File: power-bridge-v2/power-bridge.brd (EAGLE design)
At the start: 9.8 x 22.4 mm, 3 parts, among them X2 CON-MA03-2PCB_EDGE

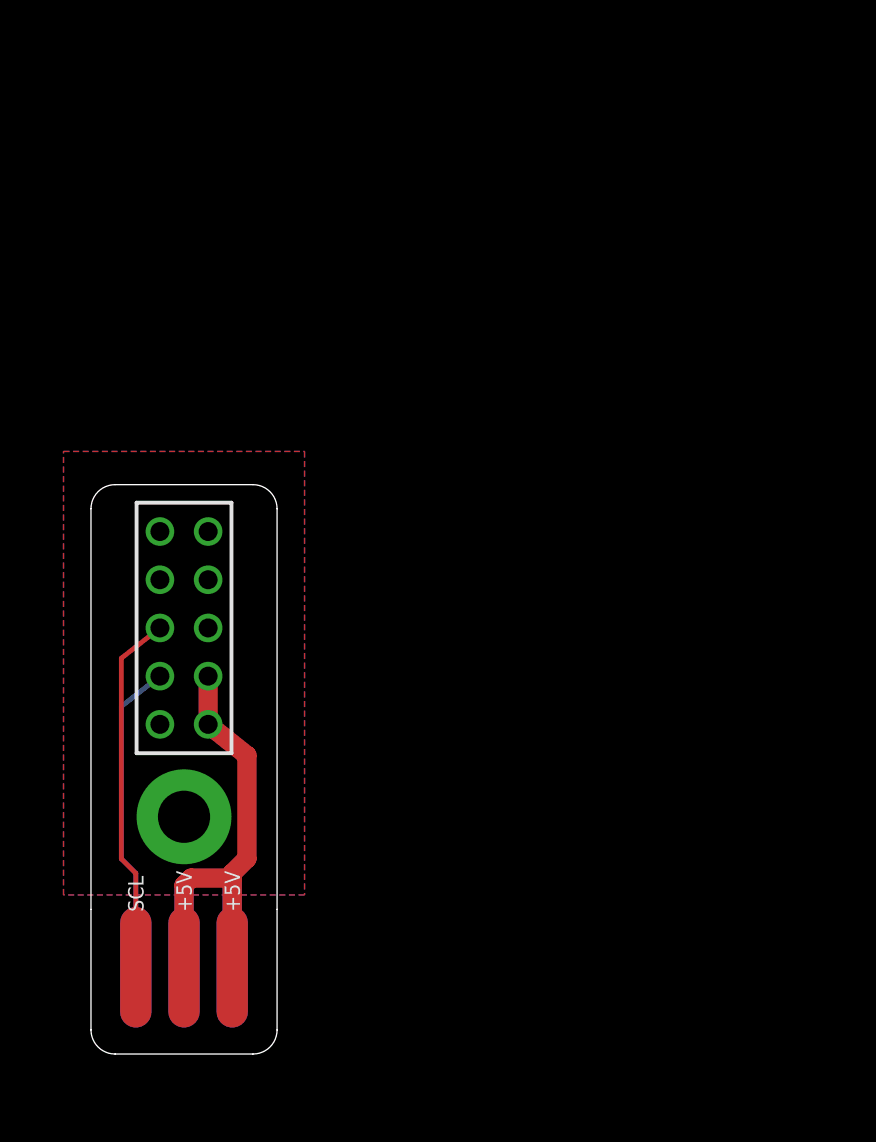
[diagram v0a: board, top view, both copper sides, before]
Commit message: Add power bridge v3
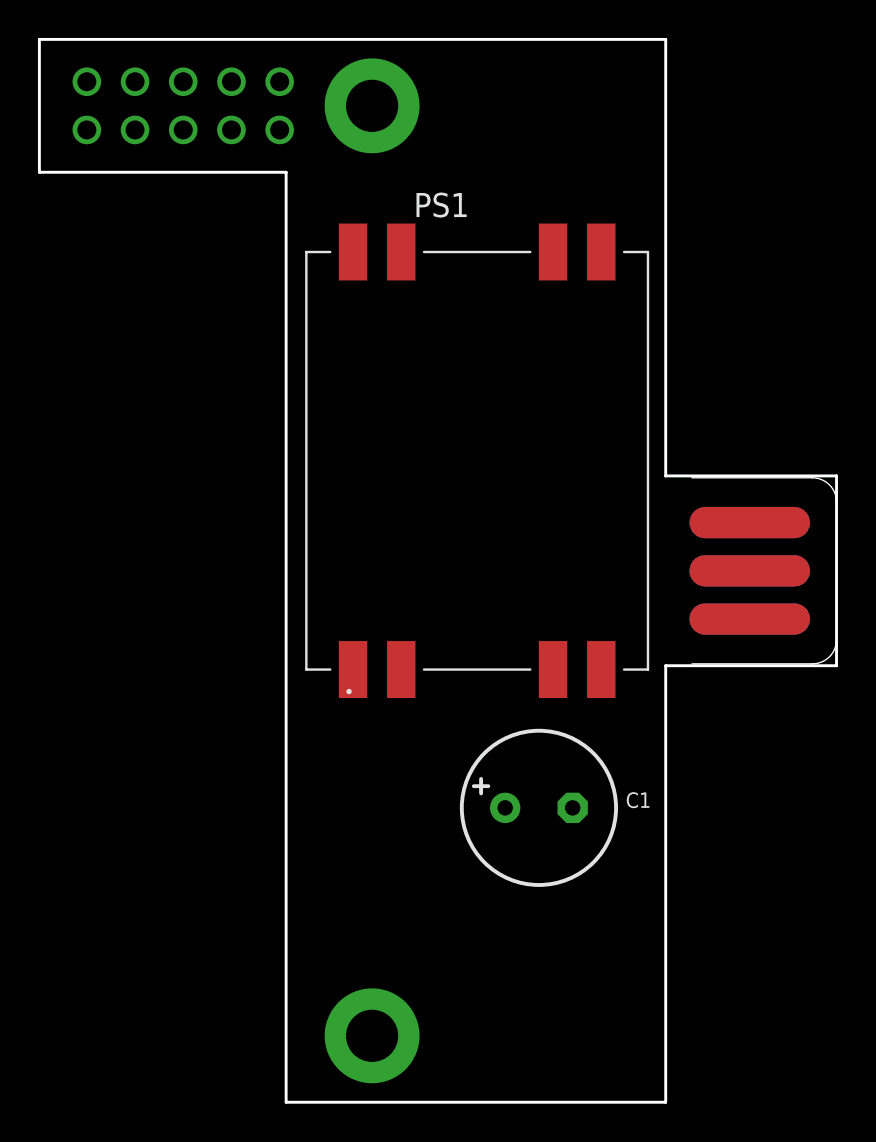
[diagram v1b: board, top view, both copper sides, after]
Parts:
- added C1: 100uF, sanisimov:CELEC_3.5MM_8MM
- added PS1: (no value), sanisimov:K8801
- added U$3: MOUNTINGHOLE2.7_THICK, sanisimov:MOUNTINGHOLE_2.7_PLATED_THICK
- moved X2 42.8 mm to (42.0, 28.0), flipped to the bottom, turned to 270 degrees
- moved U$2 38.7 mm to (17.5, 52.5), flipped to the bottom, turned to 270 degrees
- moved X1 27.5 mm to (7.58, 52.5), flipped to the bottom, turned to 0 degrees
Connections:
- new net +5V: PS1.5, PS1.6, X1.2, X1.4
- net GND: now also C1.-, PS1.3, PS1.4, PS1.7, PS1.8
- net PWR: now also C1.+, PS1.1, PS1.2; no longer X1.2, X1.4
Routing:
- net PWR: track 23.7 -> 0.00 mm
- net N$2: track 19.2 -> 0.00 mm
- net N$1: track 16.6 -> 0.00 mm
- net GND: track 9.27 -> 0.00 mm
- removed copper zone on layer 1, net GND
- removed copper zone on layer 16, net GND
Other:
- board size 9.8 x 22.4 mm -> 42 x 56 mm
- board text removed: "+5V"
- board text removed: "GND"
- board text removed: "SCL"
- board text removed: "SDA"
